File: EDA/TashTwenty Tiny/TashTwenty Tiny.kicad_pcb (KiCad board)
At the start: 2 copper layers, 56.6 x 57.7 mm, 31 parts, among them J1 SD_Card, J2 IDC20, J3 Conn_01x02, Q1 BC337, U1 PIC16F1825-IP, U2 74ACT08, U3 MCP1700-3302E_TO92

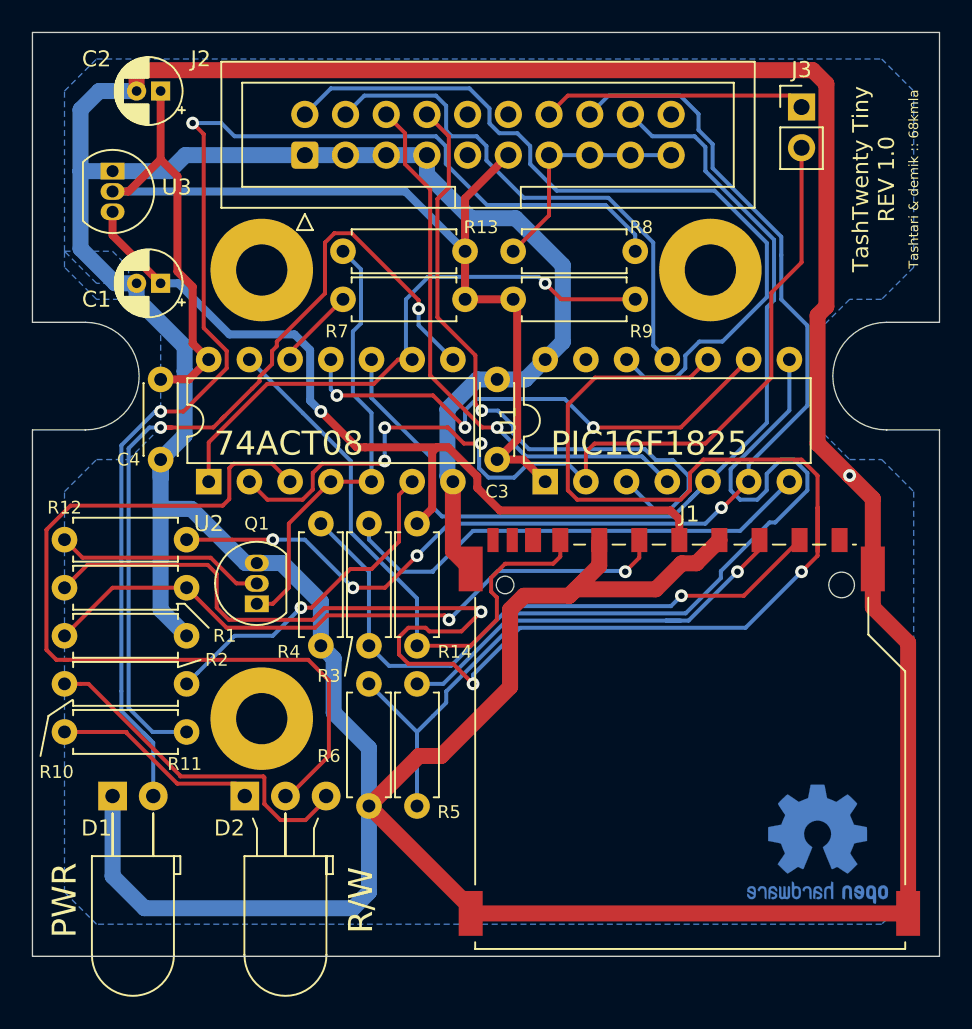
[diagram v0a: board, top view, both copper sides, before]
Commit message: added build order on silkscreen
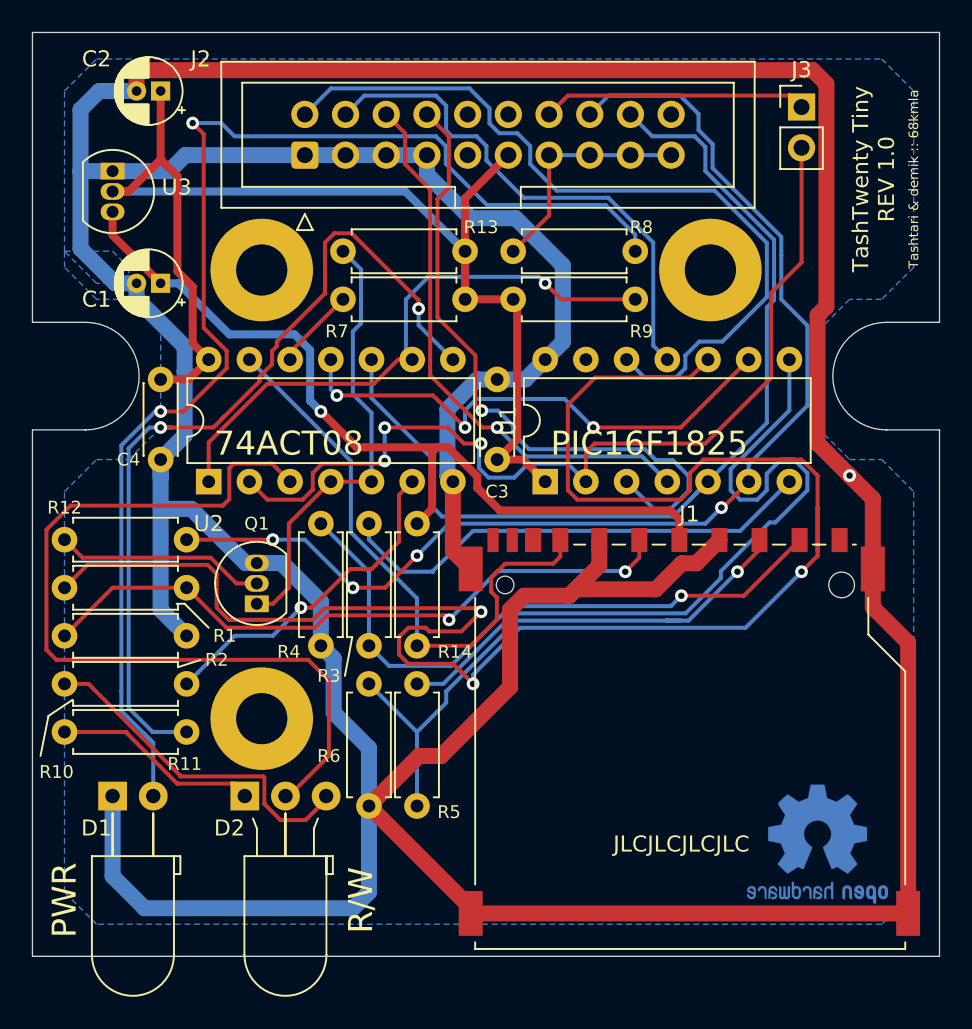
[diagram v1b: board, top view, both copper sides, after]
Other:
- board text added: "JLCJLCJLCJLC"
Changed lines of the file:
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@@
   (general
     (thickness 1.6)
-    (drawings 24)
+    (drawings 25)
     (tracks 539)
     (zones 0)
@@
   (layers
     (0 F.Cu signal)
-    (31 B.Cu signal)
+    (31 B.Cu signal hide)
     (32 B.Adhes user)
     (33 F.Adhes user)
@@
       (outputformat 1)
       (mirror false)
-      (drillshape 1)
+      (drillshape 0)
       (scaleselection 1)
       (outputdirectory ""))
@@
     (pad 3 thru_hole circle (at 0 2.54 90) (size 1.7 1.7) (drill 1) (layers *.Cu *.Mask)
       (net 2 GND))
-    (pad 1 thru_hole roundrect (at 0 0 90) (size 1.7 1.7) (drill 1) (layers *.Cu *.Mask) (roundrect_rratio 0.147059)
+    (pad 1 thru_hole roundrect (at 0 0 90) (size 1.7 1.7) (drill 1) (layers *.Cu *.Mask) (roundrect_rratio 0.1470588235294118)
       (net 2 GND))
     (model ${KISYS3DMOD}/Connector_IDC.3dshapes/IDC-Header_2x10_P2.54mm_Vertical.wrl
@@
     (pad 1 thru_hole circle (at 0 0) (size 6.4 6.4) (drill 3.2) (layers *.Cu *.Mask))
   )
+  (gr_text JLCJLCJLCJLC (at 167.5 120) (layer F.SilkS)
+    (effects (font (size 1 1) (thickness 0.15)))
+  )
   (gr_line (start 137.5 108.5) (end 136.08 108.96) (layer F.SilkS) (width 0.12))
